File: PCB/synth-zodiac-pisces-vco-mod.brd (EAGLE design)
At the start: 76.1 x 72.4 mm, 18 parts

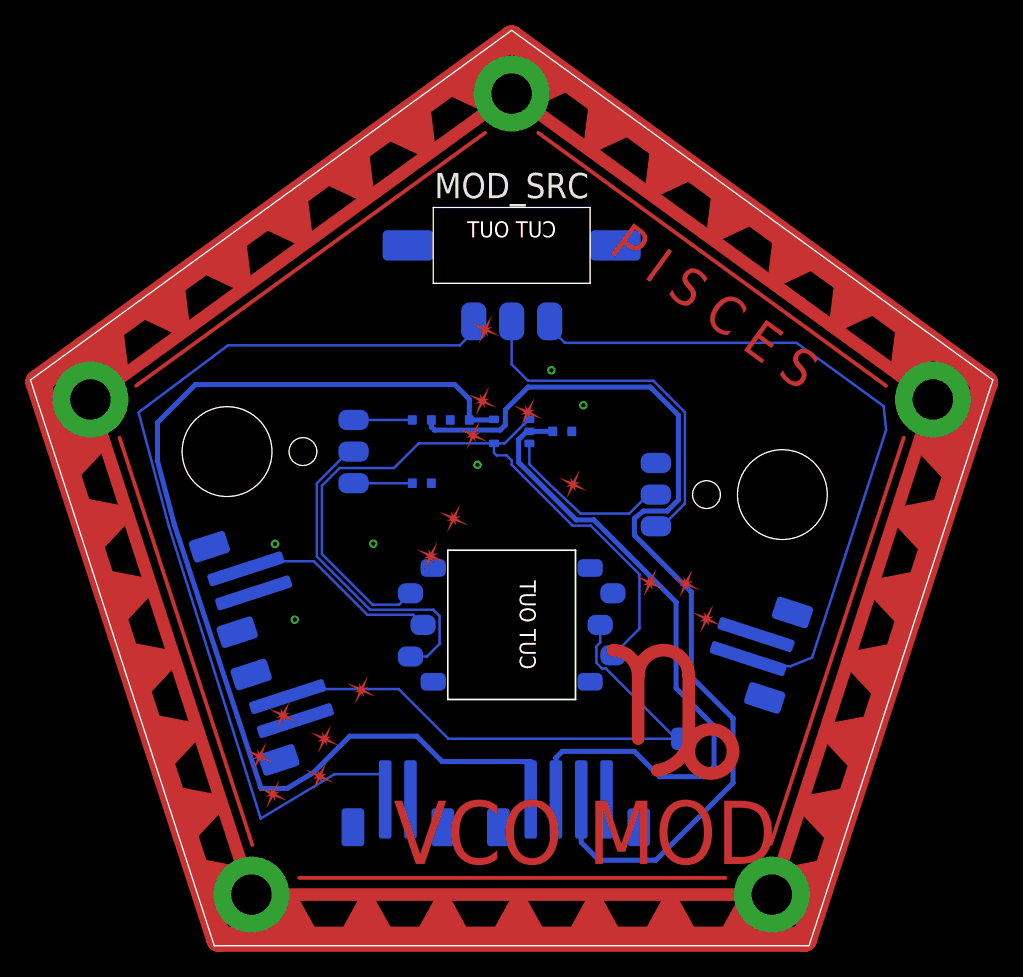
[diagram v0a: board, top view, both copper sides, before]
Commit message: Almost ready for FAB.
Sagittarius was mis-spelled, renamed it.  Taurus is still WIP.
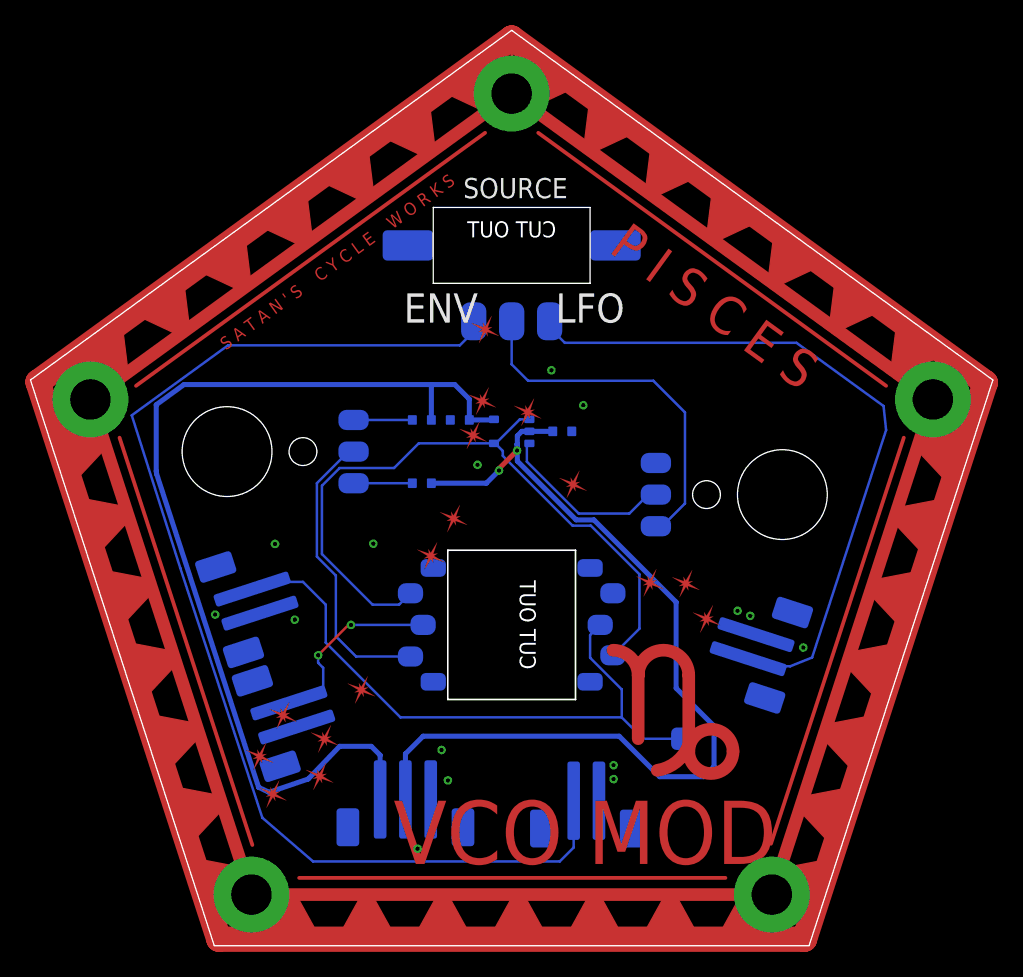
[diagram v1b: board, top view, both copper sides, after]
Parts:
- removed EG, PWM_CV, VCO_MOD: 2-pin, VT, SMT, con-jst:B2B-PH-SM4
- added EG_IN, MOD2VCO, PWM2VCO: 2-pin, VT, SMT, con-jst:B2B-PH-SM4
- PWR: value (none) -> JST, 3P, VT, SMT; device con-jst:B4B-PH-SM4 -> con-jst:B3B-PH-SM4
- R1: value 47.5R -> 12K
- moved PWR 12.9 mm to (29.6, 10.0)
- renumbered AMP to U1, C41 to C1, C42 to C2, LFO to LFO_IN, MOD_SRC to SOURCE, R70 to R2, R71 to R1
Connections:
- net LFO_CV renamed LFO
- removed net +5V: PWR.3, R1.1
- net +9V: now also R1.1
- net -9V: now also R2.2
- net EG: now also EG_IN.1; no longer EG.1
- net GND: now also EG_IN.2, MOD2VCO.2, PWM2VCO.2, PWR.3; no longer EG.2, PWM_CV.2, PWR.4, R2.2, VCO_MOD.2
- net PWM_CV: now also PWM2VCO.1; no longer PWM_CV.1
- net VCO_MOD_CV: now also MOD2VCO.1; no longer VCO_MOD.1
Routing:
- net +5V: track 76.6 -> 0.00 mm
- net -9V: track 53.2 -> 75.1 mm, vias 0 -> 2
- net EG: track 75.9 -> 93.6 mm
- net +9V: track 86.9 -> 78.5 mm
- net VCO_MOD_CV: track 45.0 -> 49.8 mm
- net N$100: track 26.3 -> 23.2 mm
- net PWM_CV: track 16.3 -> 15.4 mm, vias 0 -> 2
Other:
- board text added: "ENV"
- board text added: "LFO"
- board text added: "Rev. A"
- board text added: "S A T A N ' S C Y C L E W O R K S"

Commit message: Work in progress for rev A,  VCO rev.B
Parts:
- added PWMADJ: JST, SH, 2P, con-jst:BM02B-SRSS-TB
- EG_IN, LFO_IN, MOD2VCO, PWM2VCO: value 2-pin, VT, SMT -> JST, SH, 2P; device con-jst:B2B-PH-SM4 -> con-jst:BM02B-SRSS-TB
- PWR: value JST, 3P, VT, SMT -> JST SM 3P; device con-jst:B3B-PH-SM4 -> con-jst:BM03B-SRSS-TB
- SRC: value SPDT -> (none)
- moved CP_VCO_MOD 8.85 mm to (43.4, 14.9), turned to 180 degrees
- moved PWR 7.81 mm to (37.2, 11.8)
- moved PWM2VCO 4.70 mm to (18.8, 22.9)
- moved U1 3.81 mm to (41.8, 41.0)
- moved C2 3.41 mm to (45.4, 41.0)
- moved PULSE_WIDTH 2.90 mm to (37.9, 23.1)
- moved EG_IN 2.10 mm to (44.8, 11.8)
- moved MOD2VCO 2.06 mm to (17.0, 28.8)
- moved LFO_IN 1.65 mm to (57.5, 24.0)
- moved GLYPH 0.60 mm to (51.6, 19.0)
- moved C1 0.20 mm to (33.7, 42.2)
- renumbered SOURCE to SRC
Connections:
- removed net N$100: PULSE_WIDTH.3, PWM.C
- new net PWM_ADJ: PULSE_WIDTH.3, PWM.C, PWMADJ.1
- net GND: now also PWMADJ.2
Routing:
- net PWM_ADJ: track 0.00 -> 34.5 mm, vias 0 -> 2
- net +9V: track 78.5 -> 52.9 mm, vias 0 -> 2
- net N$100: track 23.2 -> 0.00 mm
- net LFO: track 55.3 -> 35.6 mm
- net -9V: track 75.1 -> 59.7 mm, vias 2 -> 4
- net EG: track 93.6 -> 83.2 mm, vias 0 -> 2
- net N$86: track 14.1 -> 8.19 mm
- net MOD_CORE: track 56.3 -> 61.9 mm, vias 0 -> 2
- net VCO_MOD_CV: track 49.8 -> 47.2 mm
- net PWM_CV: track 15.4 -> 13.9 mm
- net VCO_SRC: track 28.9 -> 28.1 mm
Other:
- board text added: "%"

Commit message: Perhaps final Rev. A?
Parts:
- PULSE_WIDTH: value DPDT -> Switch, DPDT; device switch-thd:CK_OS202013MT5-PNL-SMT -> switch-thd:CK_OS202013MT5-PNL-SMT-2
- SRC: device switch-thd:SS-12-F45-PNL-SMT -> switch-thd:SS-12-F45-PNL-SMT-2
- moved CP_VCO_MOD 2.00 mm to (45.4, 14.9)
- moved SRC 0.50 mm to (38.0, 56.5), flipped to the top
- flipped PULSE_WIDTH to the top, turned to 90 degrees
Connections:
- net EG: now also SRC.A; no longer SRC.B
- net GND: now also SRC.MTG3, SRC.MTG4
- net LFO: now also SRC.B; no longer SRC.A
- net MOD_CORE: now also PULSE_WIDTH.5C; no longer PULSE_WIDTH.6
- net PWM_ADJ: now also PULSE_WIDTH.2C; no longer PULSE_WIDTH.3
- net PWM_CV: now also PULSE_WIDTH.3; no longer PULSE_WIDTH.2C
- net VCO_MOD_CV: now also PULSE_WIDTH.6; no longer PULSE_WIDTH.5C
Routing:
- net MOD_CORE: track 61.9 -> 66.7 mm, vias 2 -> 0
- net LFO: track 35.6 -> 38.5 mm
- net EG: track 83.2 -> 85.8 mm
- net VCO_MOD_CV: track 47.2 -> 49.6 mm
- net VCO_SRC: track 28.1 -> 29.5 mm
- net PWM_ADJ: track 34.5 -> 35.6 mm
